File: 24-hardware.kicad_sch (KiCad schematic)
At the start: 12 parts, among them J1 USB_C_Receptacle_USB2.0_14P, U1 ESP32-C3-WROOM-02, U2 AP2112K-3.3, U3 TFT_ST7735_SD

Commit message: added screen
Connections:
- net rst: now reaches U1.10 (IO10)
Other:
- moved on the sheet: R3
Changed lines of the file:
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@@
-	)
-	(junction
-		(at 83.82 53.34)
-		(diameter 0)
-		(color 0 0 0 0)
 	)
 	(junction
@@
 		(color 0 0 0 0)
 	)
+	(junction
+		(at 83.82 52.07)
+		(diameter 0)
+		(color 0 0 0 0)
+	)
 	(wire
 		(pts
@@
 	(wire
 		(pts
-			(xy 83.82 53.34) (xy 83.82 68.58)
-		)
-		(stroke
-			(width 0)
-			(type default)
-		)
-	)
-	(wire
-		(pts
 			(xy 62.23 49.53) (xy 64.77 49.53)
 		)
@@
 	(wire
 		(pts
+			(xy 83.82 52.07) (xy 83.82 68.58)
+		)
+		(stroke
+			(width 0)
+			(type default)
+		)
+	)
+	(wire
+		(pts
 			(xy 90.17 58.42) (xy 95.25 58.42)
 		)
@@
 	(wire
 		(pts
-			(xy 83.82 52.07) (xy 83.82 53.34)
-		)
-		(stroke
-			(width 0)
-			(type default)
-		)
-	)
-	(wire
-		(pts
 			(xy 90.17 60.96) (xy 95.25 60.96)
 		)
@@
 	(wire
 		(pts
+			(xy 95.25 52.07) (xy 95.25 53.34)
+		)
+		(stroke
+			(width 0)
+			(type default)
+		)
+	)
+	(wire
+		(pts
 			(xy 64.77 38.1) (xy 64.77 49.53)
 		)
@@
 	(wire
 		(pts
-			(xy 93.98 53.34) (xy 95.25 53.34)
+			(xy 92.71 52.07) (xy 95.25 52.07)
 		)
 		(stroke
@@
 	(wire
 		(pts
-			(xy 86.36 53.34) (xy 83.82 53.34)
+			(xy 85.09 52.07) (xy 83.82 52.07)
+		)
+		(stroke
+			(width 0)
+			(type default)
+		)
+	)
+	(wire
+		(pts
+			(xy 88.9 73.66) (xy 95.25 73.66)
 		)
 		(stroke
@@
 	(label "mosi"
 		(at 90.17 63.5 0)
+		(effects
+			(font
+				(size 1.27 1.27)
+			)
+			(justify left bottom)
+		)
+	)
+	(label "rst"
+		(at 88.9 73.66 0)
 		(effects
 			(font
@@
 	(symbol
 		(lib_id "Device:R")
-		(at 90.17 53.34 90)
+		(at 88.9 52.07 90)
 		(unit 1)
 		(exclude_from_sim no)
@@
 		(dnp no)
 		(property "Reference" "R3"
-			(at 90.17 51.308 90)
+			(at 88.9 50.038 90)
 			(effects
 				(font
@@
 		)
 		(property "Value" "10k"
-			(at 90.17 53.34 90)
+			(at 88.9 52.07 90)
 			(effects
 				(font
@@
 		)
 		(property "Footprint" ""
-			(at 90.17 55.118 90)
+			(at 88.9 53.848 90)
 			(effects
 				(font
@@
 		)
 		(property "Datasheet" "~"
-			(at 90.17 53.34 0)
+			(at 88.9 52.07 0)
 			(effects
 				(font
@@
 		)
 		(property "Description" "Resistor"
-			(at 90.17 53.34 0)
-			(effects
-				(font
+			(at 88.9 52.07 0)
+			(effects
+				(font

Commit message: added screen
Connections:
- net +3V3: now also U3.1 (3V3)
- net miso: now also U3.11 (SD_MISO)
- net mosi: now also U3.10 (SD_MOSI), U3.6 (LCD_MOSI)
- net rst: now also U3.4 (EN)
- net sck: now also U3.12 (SD_SCK)
- net c2: now reaches U1.8 (IO9)
- net c2: now also U3.9 (SD_CS)
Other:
- moved on the sheet: R4
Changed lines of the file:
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@@
+	(wire
+		(pts
+			(xy 161.29 57.15) (xy 166.37 57.15)
+		)
+		(stroke
+			(width 0)
+			(type default)
+		)
+	)
+	(wire
+		(pts
+			(xy 90.17 74.93) (xy 90.17 73.66)
+		)
+		(stroke
+			(width 0)
+			(type default)
+		)
+	)
 	(wire
 		(pts
@@
 	(wire
 		(pts
+			(xy 161.29 59.69) (xy 166.37 59.69)
+		)
+		(stroke
+			(width 0)
+			(type default)
+		)
+	)
+	(wire
+		(pts
 			(xy 45.72 62.23) (xy 45.72 64.77)
 		)
@@
 	(wire
 		(pts
+			(xy 90.17 73.66) (xy 95.25 73.66)
+		)
+		(stroke
+			(width 0)
+			(type default)
+		)
+	)
+	(wire
+		(pts
 			(xy 83.82 52.07) (xy 83.82 68.58)
 		)
@@
 	(wire
 		(pts
+			(xy 161.29 54.61) (xy 166.37 54.61)
+		)
+		(stroke
+			(width 0)
+			(type default)
+		)
+	)
+	(wire
+		(pts
 			(xy 114.3 24.13) (xy 124.46 24.13)
 		)
@@
 	(wire
 		(pts
-			(xy 86.36 68.58) (xy 83.82 68.58)
+			(xy 85.09 68.58) (xy 83.82 68.58)
 		)
 		(stroke
@@
 	(wire
 		(pts
+			(xy 91.44 71.12) (xy 95.25 71.12)
+		)
+		(stroke
+			(width 0)
+			(type default)
+		)
+	)
+	(wire
+		(pts
 			(xy 30.48 85.09) (xy 30.48 87.63)
 		)
@@
 	(wire
 		(pts
+			(xy 132.08 59.69) (xy 137.16 59.69)
+		)
+		(stroke
+			(width 0)
+			(type default)
+		)
+	)
+	(wire
+		(pts
 			(xy 85.09 52.07) (xy 83.82 52.07)
 		)
@@
 	(wire
 		(pts
-			(xy 88.9 73.66) (xy 95.25 73.66)
+			(xy 133.35 54.61) (xy 137.16 54.61)
+		)
+		(stroke
+			(width 0)
+			(type default)
+		)
+	)
+	(wire
+		(pts
+			(xy 82.55 74.93) (xy 90.17 74.93)
 		)
 		(stroke
@@
 	(wire
 		(pts
-			(xy 93.98 68.58) (xy 95.25 68.58)
+			(xy 161.29 62.23) (xy 165.1 62.23)
+		)
+		(stroke
+			(width 0)
+			(type default)
+		)
+	)
+	(wire
+		(pts
+			(xy 92.71 68.58) (xy 95.25 68.58)
 		)
 		(stroke
@@
 	(wire
 		(pts
+			(xy 148.59 38.1) (xy 148.59 43.18)
+		)
+		(stroke
+			(width 0)
+			(type default)
+		)
+	)
+	(wire
+		(pts
 			(xy 45.72 57.15) (xy 45.72 59.69)
 		)
@@
 			(width 0)
 			(type default)
+		)
+	)
+	(label "miso"
+		(at 166.37 59.69 180)
+		(effects
+			(font
+				(size 1.27 1.27)
+			)
+			(justify right bottom)
+		)
+	)
+	(label "c2"
+		(at 166.37 54.61 180)
+		(effects
+			(font
+				(size 1.27 1.27)
+			)
+			(justify right bottom)
+		)
+	)
+	(label "c2"
+		(at 91.44 71.12 0)
+		(effects
+			(font
+				(size 1.27 1.27)
+			)
+			(justify left bottom)
+		)
+	)
+	(label "sck"
+		(at 165.1 62.23 180)
+		(effects
+			(font
+				(size 1.27 1.27)
+			)
+			(justify right bottom)
+		)
+	)
+	(label "rst"
+		(at 133.35 54.61 0)
+		(effects
+			(font
+				(size 1.27 1.27)
+			)
+			(justify left bottom)
 		)
 	)
@@
 		)
 	)
+	(label "mosi"
+		(at 166.37 57.15 180)
+		(effects
+			(font
+				(size 1.27 1.27)
+			)
+			(justify right bottom)
+		)
+	)
 	(label "sck"
 		(at 90.17 58.42 0)
@@
 		)
 	)
+	(label "mosi"
+		(at 132.08 59.69 0)
+		(effects
+			(font
+				(size 1.27 1.27)
+			)
+			(justify left bottom)
+		)
+	)
 	(label "cs"
 		(at 90.17 66.04 0)
@@
 	)
 	(label "rst"
-		(at 88.9 73.66 0)
+		(at 82.55 74.93 0)
 		(effects
 			(font
@@
 	(symbol
 		(lib_id "power:+3V3")
+		(at 148.59 38.1 0)
+		(unit 1)
+		(exclude_from_sim no)
+		(in_bom yes)
+		(on_board yes)
+		(dnp no)
+		(fields_autoplaced yes)
+		(property "Reference" "#PWR09"
+			(at 148.59 41.91 0)
+			(effects
+				(font
+					(size 1.27 1.27)
+				)
+				(hide yes)
+			)
+		)
+		(property "Value" "+3V3"
+			(at 148.59 33.02 0)
+			(effects
+				(font
+					(size 1.27 1.27)
+				)
+			)
+		)
+		(property "Footprint" ""
+			(at 148.59 38.1 0)
+			(effects
+				(font
+					(size 1.27 1.27)
+				)
+				(hide yes)
+			)
+		)
+		(property "Datasheet" ""
+			(at 148.59 38.1 0)
+			(effects
+				(font
+					(size 1.27 1.27)
+				)
+				(hide yes)
+			)
+		)
+		(property "Description" "Power symbol creates a global label with name \"+3V3\""
+			(at 148.59 38.1 0)
+			(effects
+				(font
+					(size 1.27 1.27)
+				)
+				(hide yes)
+			)
+		)
+		(pin "1"
+		)
+		(instances
+			(project "24-hardware"
+				(path "/cff53a01-7c0d-4fba-a887-0c9345fcd163"
+					(reference "#PWR09")
+					(unit 1)
+				)
+			)
+		)
+	)
+	(symbol
+		(lib_id "power:+3V3")
 		(at 110.49 21.59 0)
 		(unit 1)
@@
 	(symbol
 		(lib_id "Device:R")
-		(at 90.17 68.58 270)
+		(at 88.9 68.58 270)
 		(unit 1)
 		(exclude_from_sim no)
@@
 		(dnp no)
 		(property "Reference" "R4"
-			(at 90.17 71.374 90)
+			(at 88.9 71.374 90)
 			(effects
 				(font
@@
 		)
 		(property "Value" "10k"
-			(at 90.424 68.58 90)
+			(at 88.9 68.58 90)
 			(effects
 				(font
@@
 		)
 		(property "Footprint" ""
-			(at 90.17 66.802 90)
+			(at 88.9 66.802 90)
 			(effects
 				(font
@@
 		)
 		(property "Datasheet" "~"
-			(at 90.17 68.58 0)
+			(at 88.9 68.58 0)
 			(effects
 				(font
@@
 		)
 		(property "Description" "Resistor"
-			(at 90.17 68.58 0)
-			(effects
-				(font
+			(at 88.9 68.58 0)
+			(effects
+				(font

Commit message: addded adc
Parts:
- added SW1: SW_Push, symbol Switch:SW_Push
- added U4: PCM5102, Package_SO:TSSOP-20_4.4x6.5mm_P0.65mm, symbol Audio:PCM5102
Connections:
- net GND: now also SW1.1
- net at U1.18 (IO0): now also SW1.2
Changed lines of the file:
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@@
 		(color 0 0 0 0)
 	)
+	(junction
+		(at 71.12 49.53)
+		(diameter 0)
+		(color 0 0 0 0)
+	)
 	(wire
 		(pts
@@
 	(wire
 		(pts
+			(xy 71.12 45.72) (xy 71.12 49.53)
+		)
+		(stroke
+			(width 0)
+			(type default)
+		)
+	)
+	(wire
+		(pts
 			(xy 62.23 49.53) (xy 64.77 49.53)
 		)
@@
 	(wire
 		(pts
+			(xy 83.82 45.72) (xy 71.12 45.72)
+		)
+		(stroke
+			(width 0)
+			(type default)
+		)
+	)
+	(wire
+		(pts
 			(xy 97.79 22.86) (xy 101.6 22.86)
 		)
@@
 	(wire
 		(pts
-			(xy 67.31 49.53) (xy 72.39 49.53)
+			(xy 67.31 49.53) (xy 71.12 49.53)
+		)
+		(stroke
+			(width 0)
+			(type default)
+		)
+	)
+	(wire
+		(pts
+			(xy 93.98 45.72) (xy 93.98 48.26)
 		)
 		(stroke
@@
 	(wire
 		(pts
+			(xy 71.12 49.53) (xy 72.39 49.53)
+		)
+		(stroke
+			(width 0)
+			(type default)
+		)
+	)
+	(wire
+		(pts
 			(xy 161.29 62.23) (xy 165.1 62.23)
 		)
@@
 		(pts
 			(xy 45.72 57.15) (xy 45.72 59.69)
+		)
+		(stroke
+			(width 0)
+			(type default)
+		)
+	)
+	(wire
+		(pts
+			(xy 93.98 48.26) (xy 95.25 48.26)
 		)
 		(stroke
@@
 	)
 	(symbol
+		(lib_id "Audio:PCM5102")
+		(at 200.66 52.07 0)
+		(unit 1)
+		(exclude_from_sim no)
+		(in_bom yes)
+		(on_board yes)
+		(dnp no)
+		(fields_autoplaced yes)
+		(property "Reference" "U4"
+			(at 205.3433 34.29 0)
+			(effects
+				(font
+					(size 1.27 1.27)
+				)
+				(justify left)
+			)
+		)
+		(property "Value" "PCM5102"
+			(at 205.3433 36.83 0)
+			(effects
+				(font
+					(size 1.27 1.27)
+				)
+				(justify left)
+			)
+		)
+		(property "Footprint" "Package_SO:TSSOP-20_4.4x6.5mm_P0.65mm"
+			(at 199.39 33.02 0)
+			(effects
+				(font
+					(size 1.27 1.27)
+				)
+				(hide yes)
+			)
+		)
+		(property "Datasheet" "http://www.ti.com/lit/ds/symlink/pcm5102.pdf"
+			(at 199.39 33.02 0)
+			(effects
+				(font
+					(size 1.27 1.27)
+				)
+				(hide yes)
+			)
+		)
+		(property "Description" "2VRMS DirectPath, 112dB Audio Stereo DAC with 32-bit, 384kHz PCM Interface, TSSOP-20"
+			(at 200.66 52.07 0)
+			(effects
+				(font
+					(size 1.27 1.27)
+				)
+				(hide yes)
+			)
+		)
+		(pin "7"
+		)
+		(pin "15"
+		)
+		(pin "17"
+		)
+		(pin "10"
+		)
+		(pin "11"
+		)
+		(pin "9"
+		)
+		(pin "18"
+		)
+		(pin "6"
+		)
+		(pin "16"
+		)
+		(pin "8"
+		)
+		(pin "1"
+		)
+		(pin "2"
+		)
+		(pin "20"
+		)
+		(pin "3"
+		)
+		(pin "19"
+		)
+		(pin "12"
+		)
+		(pin "13"
+		)
+		(pin "14"
+		)
+		(pin "5"
+		)
+		(pin "4"
+		)
+		(instances
+			(project ""
+				(path "/cff53a01-7c0d-4fba-a887-0c9345fcd163"
+					(reference "U4")
+					(unit 1)
+				)
+			)
+		)
+	)
+	(symbol
 		(lib_id "Device:R")
 		(at 88.9 52.07 90)
@@
 					(unit 1)
 				)
+			)
+		)
+	)
+	(symbol
+		(lib_id "Switch:SW_Push")
+		(at 88.9 45.72 0)
+		(unit 1)
+		(exclude_from_sim no)
+		(in_bom yes)
+		(on_board yes)
+		(dnp no)
+		(property "Reference" "SW1"
+			(at 91.44 43.434 0)
+			(effects
+				(font
+					(size 1.27 1.27)
+				)
+			)
+		)
+		(property "Value" "SW_Push"
+			(at 83.82 43.18 0)
+			(effects
+				(font
+					(size 1.27 1.27)
+				)
+			)
+		)
+		(property "Footprint" ""
+			(at 88.9 40.64 0)
+			(effects
+				(font
+					(size 1.27 1.27)
+				)
+				(hide yes)
+			)
+		)
+		(property "Datasheet" "~"
+			(at 88.9 40.64 0)
+			(effects
+				(font
+					(size 1.27 1.27)
+				)
+				(hide yes)
+			)
+		)
+		(property "Description" "Push button switch, generic, two pins"
+			(at 88.9 45.72 0)
+			(effects
+				(font
+					(size 1.27 1.27)
+				)
+				(hide yes)
+			)
+		)
+		(pin "2"
+		)
+		(pin "1"
+		)
+		(instances
+			(project ""
+				(path "/cff53a01-7c0d-4fba-a887-0c9345fcd163"
+					(reference "SW1")
+					(unit 1)
+				)

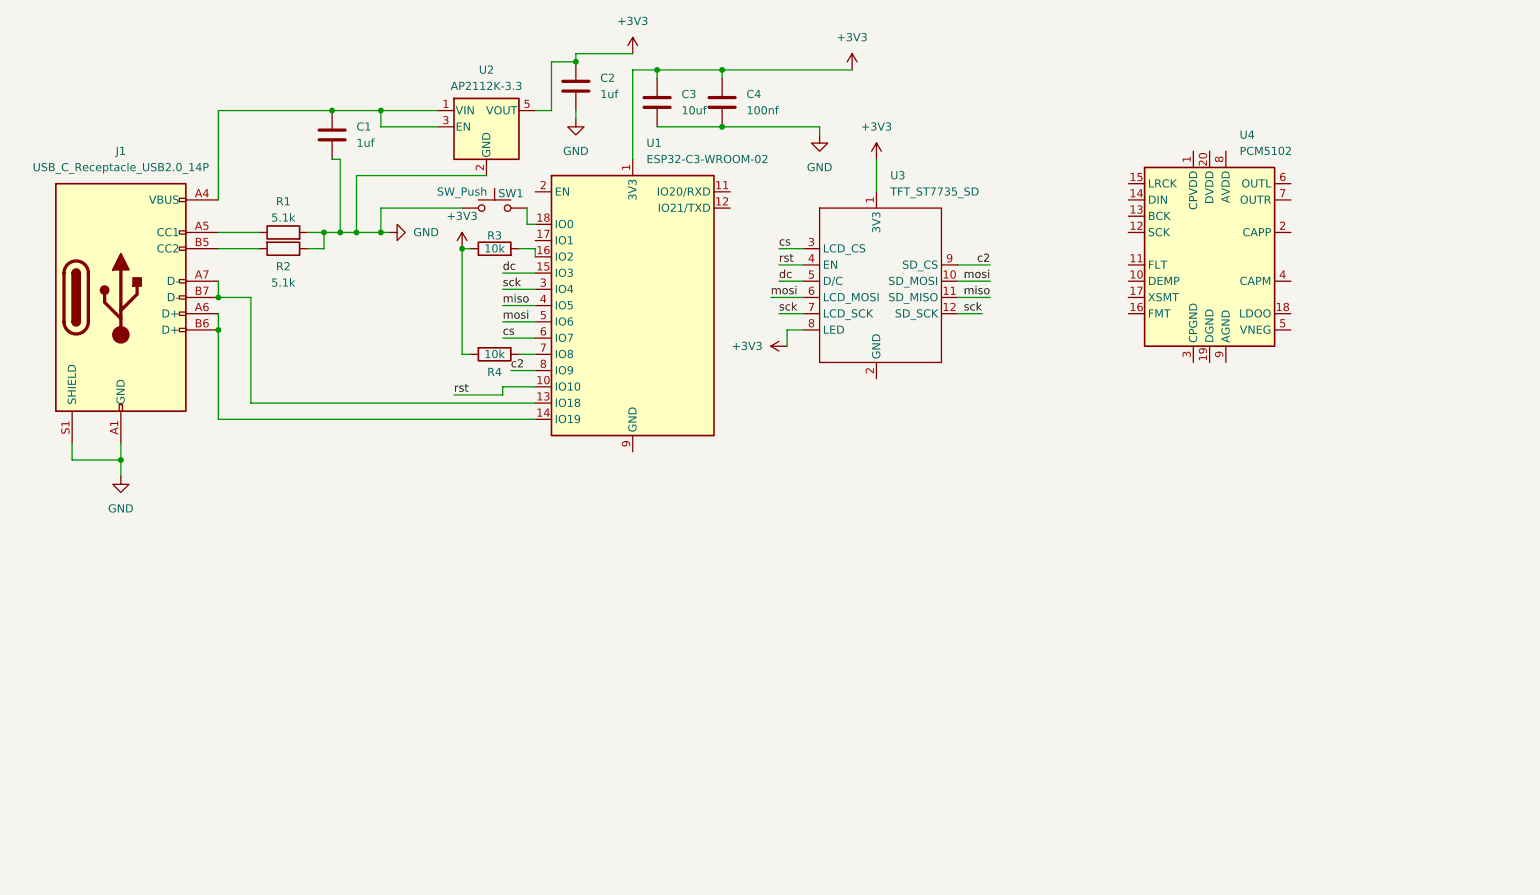
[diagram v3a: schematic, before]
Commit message: added new cpu
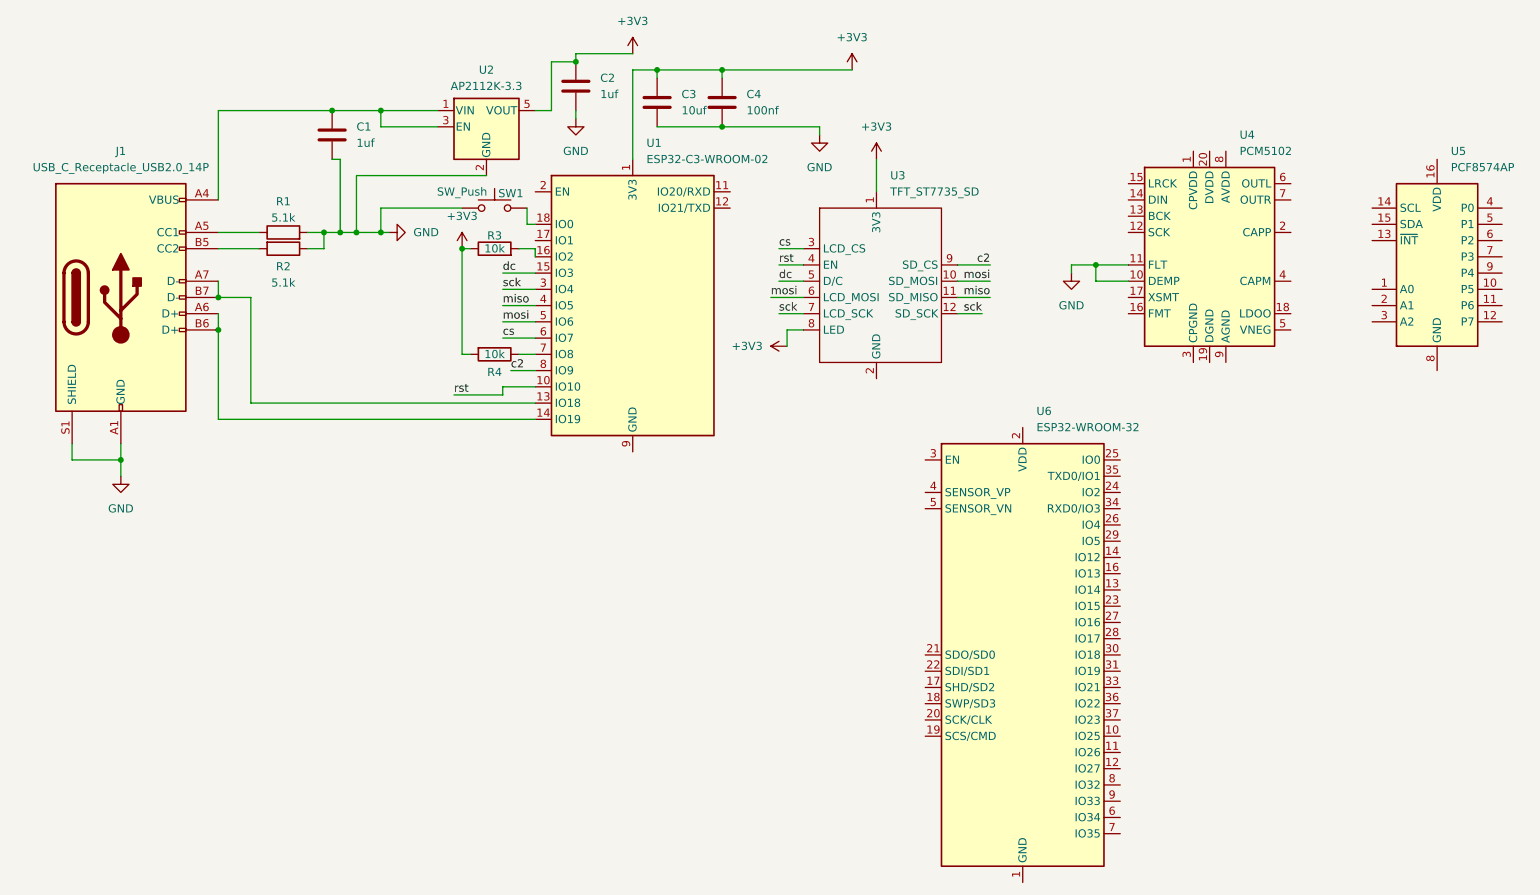
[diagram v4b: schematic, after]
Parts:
- added U5: PCF8574AP, Package_DIP:DIP-16_W7.62mm, symbol Interface_Expansion:PCF8574AP
- added U6: ESP32-WROOM-32, RF_Module:ESP32-WROOM-32, symbol RF_Module:ESP32-WROOM-32
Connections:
- net GND: now also U4.10 (DEMP), U4.11 (FLT)
- new net: U6.1 (GND), U6.15 (GND), U6.38 (GND), U6.39 (GND)

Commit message: idk
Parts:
- removed U6: ESP32-WROOM-32, RF_Module:ESP32-WROOM-32, symbol RF_Module:ESP32-WROOM-32
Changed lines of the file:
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@@
-	)
-	(symbol
-		(lib_id "RF_Module:ESP32-WROOM-32")
-		(at 171.45 115.57 0)
-		(unit 1)
-		(exclude_from_sim no)
-		(in_bom yes)
-		(on_board yes)
-		(dnp no)
-		(fields_autoplaced yes)
-		(property "Reference" "U6"
-			(at 173.5933 77.47 0)
-			(effects
-				(font
-					(size 1.27 1.27)
-				)
-				(justify left)
-			)
-		)
-		(property "Value" "ESP32-WROOM-32"
-			(at 173.5933 80.01 0)
-			(effects
-				(font
-					(size 1.27 1.27)
-				)
-				(justify left)
-			)
-		)
-		(property "Footprint" "RF_Module:ESP32-WROOM-32"
-			(at 171.45 153.67 0)
-			(effects
-				(font
-					(size 1.27 1.27)
-				)
-				(hide yes)
-			)
-		)
-		(property "Datasheet" "https://www.espressif.com/sites/default/files/documentation/esp32-wroom-32_datasheet_en.pdf"
-			(at 163.83 114.3 0)
-			(effects
-				(font
-					(size 1.27 1.27)
-				)
-				(hide yes)
-			)
-		)
-		(property "Description" "RF Module, ESP32-D0WDQ6 SoC, Wi-Fi 802.11b/g/n, Bluetooth, BLE, 32-bit, 2.7-3.6V, onboard antenna, SMD"
-			(at 171.45 115.57 0)
-			(effects
-				(font
-					(size 1.27 1.27)
-				)
-				(hide yes)
-			)
-		)
-		(pin "7"
-		)
-		(pin "27"
-		)
-		(pin "11"
-		)
-		(pin "31"
-		)
-		(pin "6"
-		)
-		(pin "9"
-		)
-		(pin "8"
-		)
-		(pin "39"
-		)
-		(pin "5"
-		)
-		(pin "21"
-		)
-		(pin "1"
-		)
-		(pin "32"
-		)
-		(pin "12"
-		)
-		(pin "10"
-		)
-		(pin "28"
-		)
-		(pin "22"
-		)
-		(pin "26"
-		)
-		(pin "34"
-		)
-		(pin "2"
-		)
-		(pin "17"
-		)
-		(pin "13"
-		)
-		(pin "4"
-		)
-		(pin "38"
-		)
-		(pin "16"
-		)
-		(pin "19"
-		)
-		(pin "14"
-		)
-		(pin "35"
-		)
-		(pin "30"
-		)
-		(pin "3"
-		)
-		(pin "23"
-		)
-		(pin "37"
-		)
-		(pin "33"
-		)
-		(pin "25"
-		)
-		(pin "29"
-		)
-		(pin "20"
-		)
-		(pin "15"
-		)
-		(pin "18"
-		)
-		(pin "36"
-		)
-		(pin "24"
-		)
-		(instances
-			(project ""
-				(path "/cff53a01-7c0d-4fba-a887-0c9345fcd163"
-					(reference "U6")
-					(unit 1)
-				)
-			)
-		)
 	)
 	(symbol
